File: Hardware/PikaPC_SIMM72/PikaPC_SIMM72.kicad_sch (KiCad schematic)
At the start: 18 parts, among them J3 Conn_02x07_Odd_Even, U1 74F521, U2 ATF1508AS

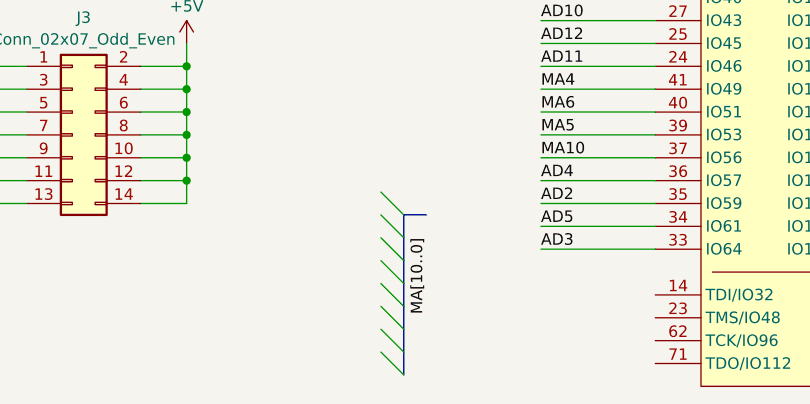
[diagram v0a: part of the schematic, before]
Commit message: ViRGE card start PCB layout
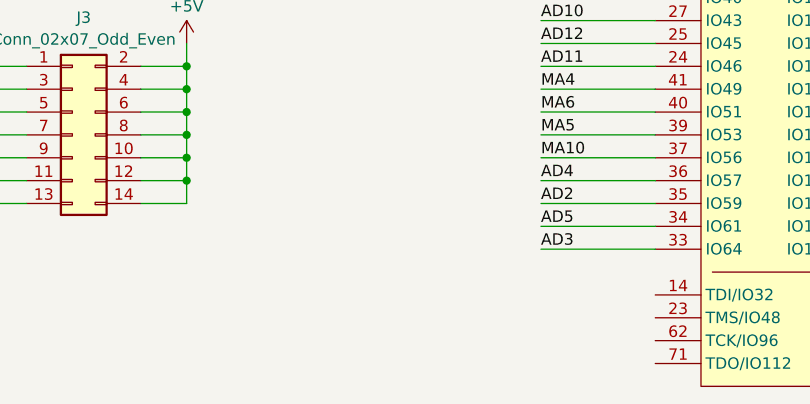
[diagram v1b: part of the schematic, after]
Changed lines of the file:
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@@
-	)
-	(bus_entry
-		(at 172.72 128.27)
-		(size 2.54 2.54)
-		(stroke
-			(width 0)
-			(type default)
-		)
 	)
 	(bus_entry
@@
 	)
 	(bus_entry
-		(at 172.72 130.81)
-		(size 2.54 2.54)
-		(stroke
-			(width 0)
-			(type default)
-		)
-	)
-	(bus_entry
-		(at 172.72 123.19)
-		(size 2.54 2.54)
-		(stroke
-			(width 0)
-			(type default)
-		)
-	)
-	(bus_entry
-		(at 172.72 133.35)
-		(size 2.54 2.54)
-		(stroke
-			(width 0)
-			(type default)
-		)
-	)
-	(bus_entry
 		(at 241.3 116.84)
 		(size 2.54 2.54)
@@
 	)
 	(bus_entry
-		(at 172.72 120.65)
-		(size 2.54 2.54)
-		(stroke
-			(width 0)
-			(type default)
-		)
-	)
-	(bus_entry
 		(at 111.76 40.64)
 		(size 2.54 2.54)
@@
 	)
 	(bus_entry
-		(at 172.72 118.11)
-		(size 2.54 2.54)
-		(stroke
-			(width 0)
-			(type default)
-		)
-	)
-	(bus_entry
 		(at 111.76 45.72)
 		(size 2.54 2.54)
@@
 	)
 	(bus_entry
-		(at 172.72 125.73)
-		(size 2.54 2.54)
-		(stroke
-			(width 0)
-			(type default)
-		)
-	)
-	(bus_entry
-		(at 172.72 135.89)
-		(size 2.54 2.54)
-		(stroke
-			(width 0)
-			(type default)
-		)
-	)
-	(bus_entry
 		(at 241.3 119.38)
 		(size 2.54 2.54)
@@
 		)
 	)
-	(bus
-		(pts
-			(xy 175.26 123.19) (xy 175.26 125.73)
-		)
-		(stroke
-			(width 0)
-			(type default)
-		)
-	)
 	(wire
 		(pts
@@
 		)
 	)
-	(bus
-		(pts
-			(xy 175.26 133.35) (xy 175.26 135.89)
-		)
-		(stroke
-			(width 0)
-			(type default)
-		)
-	)
 	(wire
 		(pts
@@
 	(bus
 		(pts
-			(xy 175.26 128.27) (xy 175.26 130.81)
-		)
-		(stroke
-			(width 0)
-			(type default)
-		)
-	)
-	(bus
-		(pts
 			(xy 111.76 40.64) (xy 111.76 43.18)
 		)
@@
 		)
 	)
-	(bus
-		(pts
-			(xy 175.26 120.65) (xy 175.26 123.19)
-		)
-		(stroke
-			(width 0)
-			(type default)
-		)
-	)
 	(wire
 		(pts
@@
 		)
 	)
-	(bus
-		(pts
-			(xy 175.26 125.73) (xy 175.26 128.27)
-		)
-		(stroke
-			(width 0)
-			(type default)
-		)
-	)
 	(wire
 		(pts
@@
 		)
 	)
-	(bus
-		(pts
-			(xy 175.26 135.89) (xy 175.26 138.43)
-		)
-		(stroke
-			(width 0)
-			(type default)
-		)
-	)
 	(wire
 		(pts
@@
 		)
 	)
-	(bus
-		(pts
-			(xy 177.8 120.65) (xy 175.26 120.65)
-		)
-		(stroke
-			(width 0)
-			(type default)
-		)
-	)
 	(wire
 		(pts
@@
 		(pts
 			(xy 25.4 83.82) (xy 38.1 83.82)
-		)
-		(stroke
-			(width 0)
-			(type default)
-		)
-	)
-	(bus
-		(pts
-			(xy 175.26 130.81) (xy 175.26 133.35)
 		)
 		(stroke
@@
 		)
 	)
-	(label "MA[10..0]"
-		(at 177.8 123.19 270)
-		(effects
-			(font
-				(size 1.27 1.27)
-			)
-			(justify right bottom)
-		)
-	)

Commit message: Prep for output
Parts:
- C1: Mouser (none) -> 187-CL21B104KACNNNC
- IO73, IO75, IO77, IO80, IO83, IO85, IO86: now not fitted; now left out of the parts list
- R1, R2, R3, R4, R5, R6, R7: Mouser (none) -> 303-0805W8J0472T5E
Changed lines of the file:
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@@
+			)
+		)
+		(property "Mouser" "303-0805W8J0472T5E"
+			(at 109.22 73.66 90)
+			(effects
+				(font
+					(size 1.27 1.27)
+				)
+				(hide yes)
 			)
 		)
@@
 		(unit 1)
 		(exclude_from_sim no)
-		(in_bom yes)
-		(on_board yes)
-		(dnp no)
+		(in_bom no)
+		(on_board yes)
+		(dnp yes)
 		(property "Reference" "IO83"
 			(at 246.38 71.12 90)
@@
 			)
 		)
+		(property "Mouser" "303-0805W8J0472T5E"
+			(at 109.22 71.12 90)
+			(effects
+				(font
+					(size 1.27 1.27)
+				)
+				(hide yes)
+			)
+		)
 		(pin "1"
 		)
@@
 			)
 		)
+		(property "Mouser" "303-0805W8J0472T5E"
+			(at 109.22 63.5 90)
+			(effects
+				(font
+					(size 1.27 1.27)
+				)
+				(hide yes)
+			)
+		)
 		(pin "1"
 		)
@@
 		(unit 1)
 		(exclude_from_sim no)
-		(in_bom yes)
-		(on_board yes)
-		(dnp no)
+		(in_bom no)
+		(on_board yes)
+		(dnp yes)
 		(property "Reference" "IO73"
 			(at 246.38 60.96 90)
@@
 		(unit 1)
 		(exclude_from_sim no)
-		(in_bom yes)
-		(on_board yes)
-		(dnp no)
+		(in_bom no)
+		(on_board yes)
+		(dnp yes)
 		(property "Reference" "IO75"
 			(at 246.38 63.5 90)
@@
 		(unit 1)
 		(exclude_from_sim no)
-		(in_bom yes)
-		(on_board yes)
-		(dnp no)
+		(in_bom no)
+		(on_board yes)
+		(dnp yes)
 		(property "Reference" "IO86"
 			(at 246.38 76.2 90)
@@
 			)
 		)
+		(property "Mouser" "303-0805W8J0472T5E"
+			(at 109.22 66.04 90)
+			(effects
+				(font
+					(size 1.27 1.27)
+				)
+				(hide yes)
+			)
+		)
 		(pin "1"
 		)
@@
 		(unit 1)
 		(exclude_from_sim no)
-		(in_bom yes)
-		(on_board yes)
-		(dnp no)
+		(in_bom no)
+		(on_board yes)
+		(dnp yes)
 		(property "Reference" "IO80"
 			(at 246.38 68.58 90)
@@
 		(unit 1)
 		(exclude_from_sim no)
-		(in_bom yes)
-		(on_board yes)
-		(dnp no)
+		(in_bom no)
+		(on_board yes)
+		(dnp yes)
 		(property "Reference" "IO77"
 			(at 246.38 66.04 90)
@@
 			)
 		)
+		(property "Mouser" "303-0805W8J0472T5E"
+			(at 109.22 76.2 90)
+			(effects
+				(font
+					(size 1.27 1.27)
+				)
+				(hide yes)
+			)
+		)
 		(pin "1"
 		)
@@
 		(unit 1)
 		(exclude_from_sim no)
-		(in_bom yes)
-		(on_board yes)
-		(dnp no)
+		(in_bom no)
+		(on_board yes)
+		(dnp yes)
 		(property "Reference" "IO85"
 			(at 246.38 73.66 90)
@@
 			)
 		)
+		(property "Mouser" "187-CL21B104KACNNNC"
+			(at 152.4 49.53 90)
+			(effects
+				(font
+					(size 1.27 1.27)
+				)
+				(hide yes)
+			)
+		)
 		(pin "2"
 		)
@@
 		(property "Description" ""
 			(at 109.22 68.58 0)
+			(effects
+				(font
+					(size 1.27 1.27)
+				)
+				(hide yes)
+			)
+		)
+		(property "Mouser" "303-0805W8J0472T5E"
+			(at 109.22 68.58 90)
 			(effects
 				(font
@@
 			(effects
 				(font
+					(size 1.27 1.27)
+				)
+				(hide yes)
+			)
+		)
+		(property "Mouser" "303-0805W8J0472T5E"
+			(at 109.22 60.96 90)
+			(effects
+				(font
